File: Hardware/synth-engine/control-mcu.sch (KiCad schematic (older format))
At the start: 76 parts

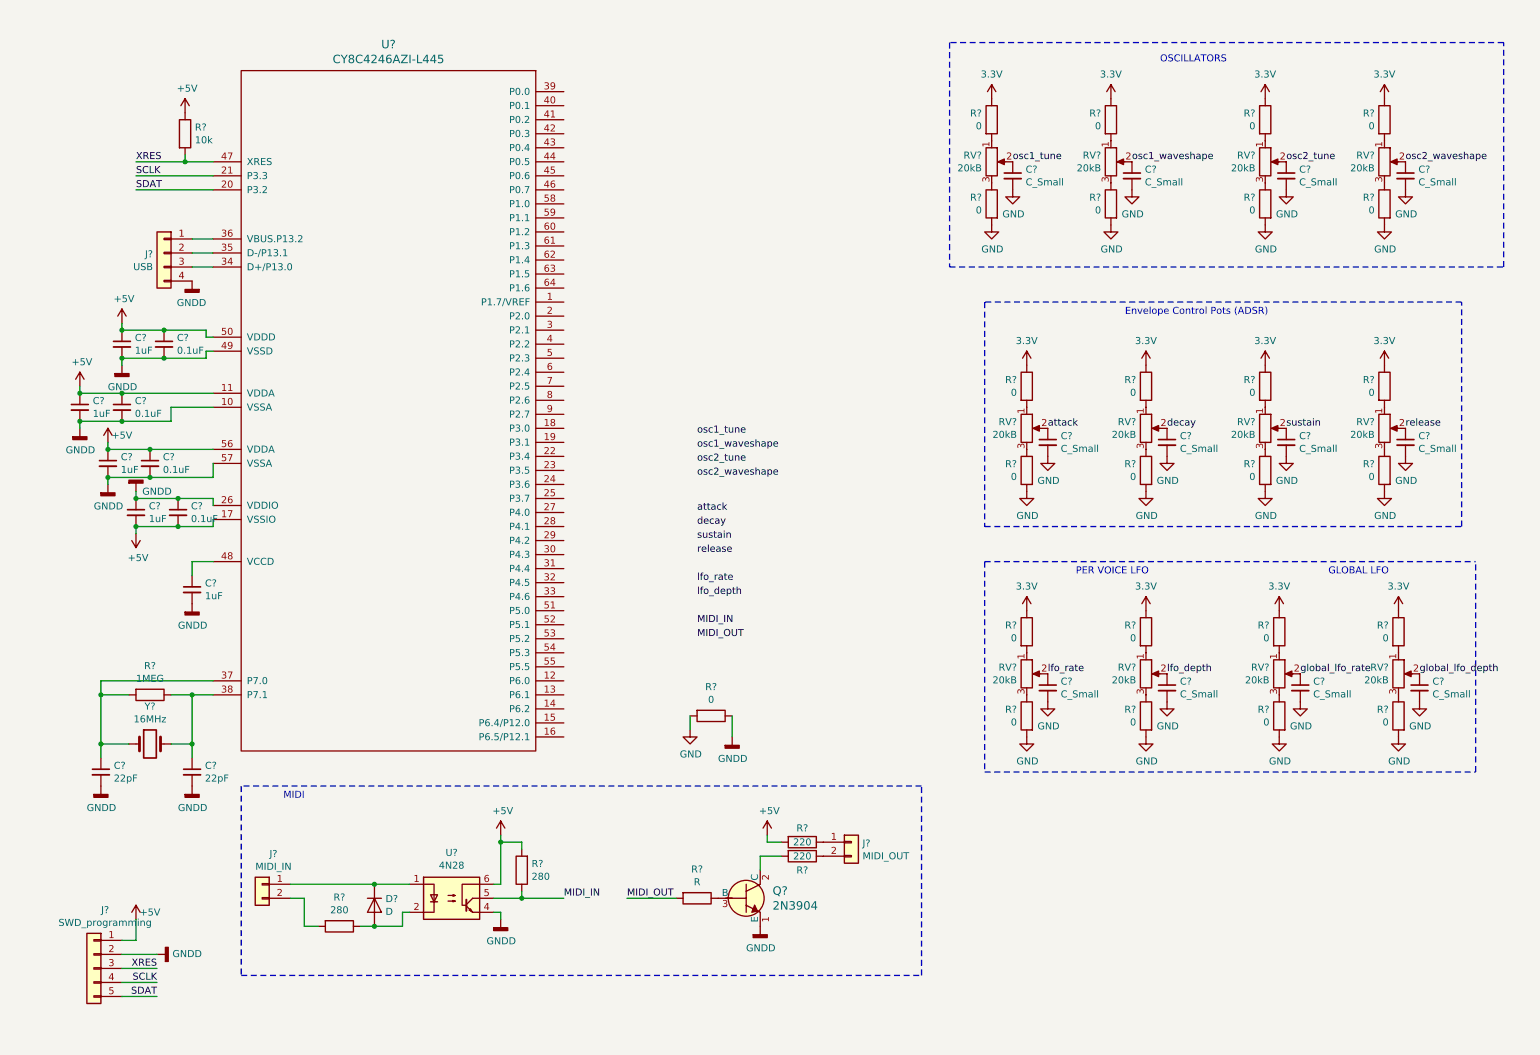
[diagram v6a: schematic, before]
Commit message: assign footprints to schematic symbols.
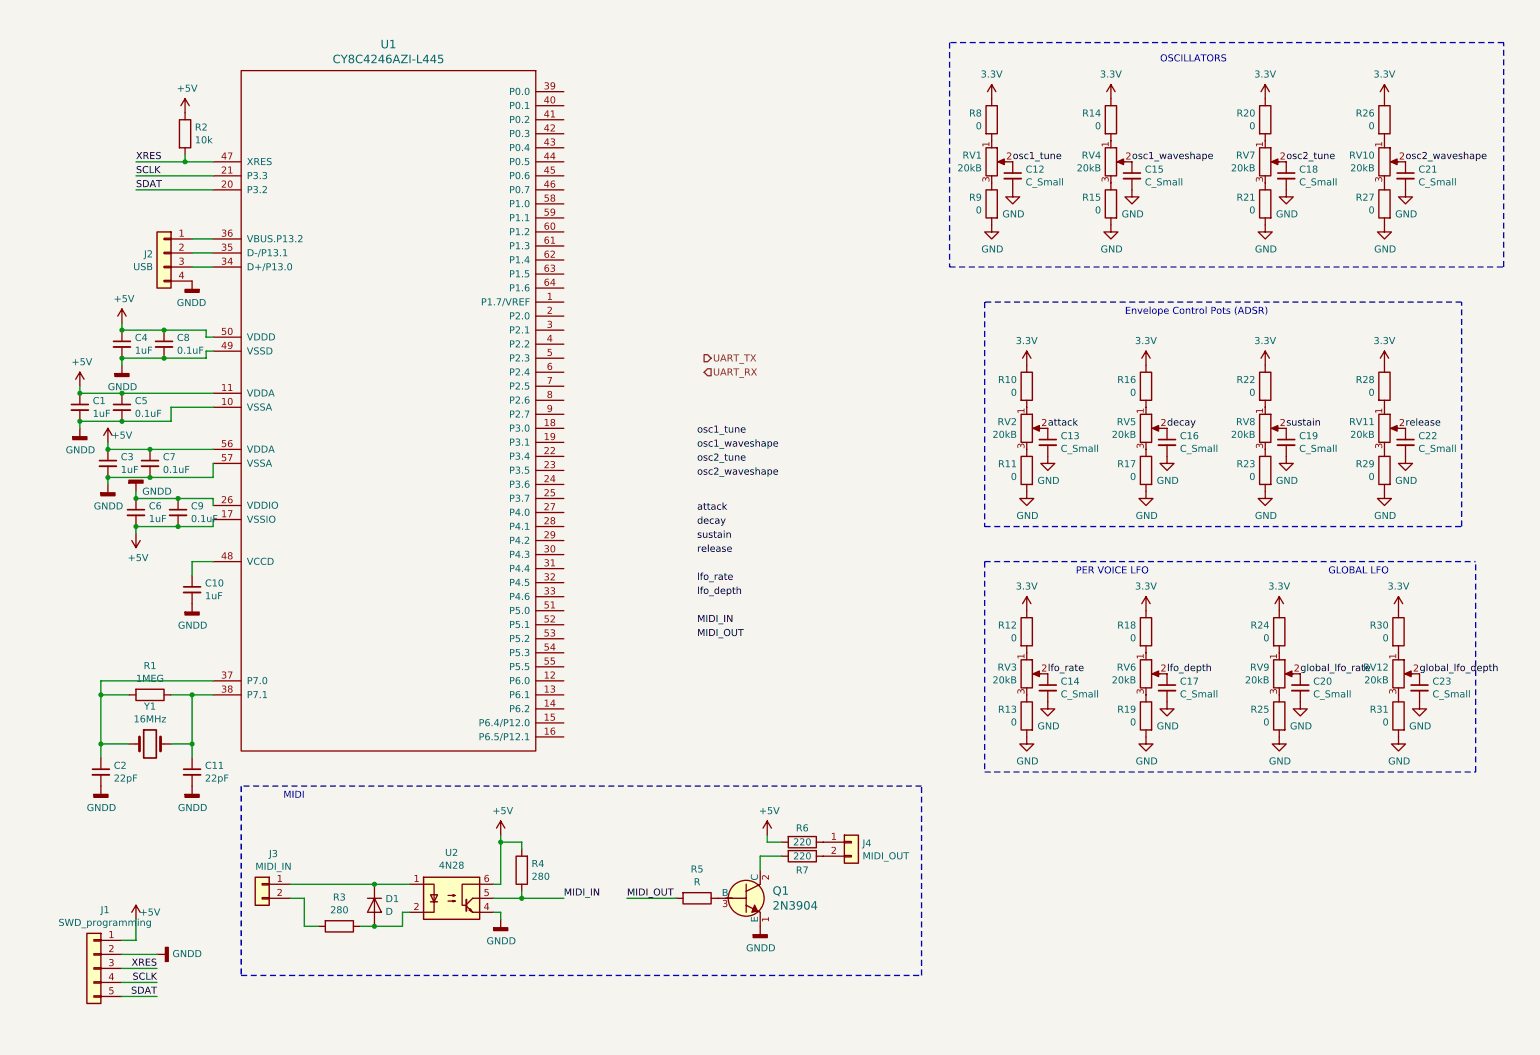
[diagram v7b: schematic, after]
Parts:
- removed R?: 0, symbol Device:R
- C1, C10, C11, C12, C13, C14, C15, C16, C17, C18, C19, C2, C20, C21, C22, C23, C3, C4, C5, C6, C7, C8, C9: renamed from C?; footprint (none) -> SparkFun-Passives:0805
- D1: renamed from D?; footprint (none) -> SparkFun-DiscreteSemi:SMA-DIODE
- J1: renamed from J?; footprint (none) -> SparkFun-Connectors:1X05
- J2: renamed from J?; footprint (none) -> SparkFun-Connectors:USB-B-PTH
- J3, J4: renamed from J?; footprint (none) -> SparkFun-Connectors:1X02
- R1, R10, R11, R12, R13, R14, R15, R16, R17, R18, R19, R2, R20, R21, R22, R23, R24, R25, R26, R27, R28, R29, R3, R30, R31, R4, R5, R6, R7, R8, R9: renamed from R?; footprint (none) -> SparkFun-Passives:0805
- RV1, RV10, RV11, RV12, RV2, RV3, RV4, RV5, RV6, RV7, RV8, RV9: renamed from RV?; footprint (none) -> Potentiometer_THT:Potentiometer_Alps_RK09K_Single_Vertical
- U1: renamed from U?; footprint (none) -> SparkFun-DigitalIC:TQFP64
- Y1: renamed from Y?; footprint (none) -> Crystal:Crystal_SMD_HC49-SD_HandSoldering
- gave numbers to parts that had none: 2

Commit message: rough placement and symbol organization. If I need to start PCB layout over from scracth, revert to this commit.
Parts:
- D1: footprint SparkFun-DiscreteSemi:SMA-DIODE -> SparkFun-DiscreteSemi:SMB-DIODE
- Q1: footprint digikey-footprints:TO-92-3 -> SparkFun-DiscreteSemi:SOT23-3
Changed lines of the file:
@@
 F 0 "D1" V 2704 6979 50  0000 L CNN
 F 1 "D" V 2795 6979 50  0000 L CNN
-F 2 "SparkFun-DiscreteSemi:SMA-DIODE" H 2750 6900 50  0001 C CNN
+F 2 "SparkFun-DiscreteSemi:SMB-DIODE" H 2750 6900 50  0001 C CNN
 F 3 "~" H 2750 6900 50  0001 C CNN
 	1    2750 6900
@@
 F 0 "Q1" H 5588 6903 60  0000 L CNN
 F 1 "2N3904" H 5588 6797 60  0000 L CNN
-F 2 "digikey-footprints:TO-92-3" H 5600 7050 60  0001 L CNN
+F 2 "SparkFun-DiscreteSemi:SOT23-3" H 5600 7050 60  0001 L CNN
 F 3 "https://my.centralsemi.com/get_document.php?cmp=1&mergetype=pd&mergepath=pd&pdf_id=LSSGP072.PDF" H 5600 7150 60  0001 L CNN
 F 4 "2N3904CS-ND" H 5600 7250 60  0001 L CNN "Digi-Key_PN"
@@
 Text Label 5050 3850 0    50   ~ 0
 osc2_waveshape
-Wire Wire Line
-	1600 2150 1450 2150
-Wire Wire Line
-	1450 2250 1600 2250
-Wire Wire Line
-	1600 2350 1450 2350
 Text HLabel 5100 3000 2    50   Output ~ 0
 UART_TX
 Text HLabel 5100 3100 2    50   Input ~ 0
 UART_RX
+Wire Wire Line
+	1450 2150 1600 2150
+Wire Wire Line
+	1450 2250 1600 2250
+Wire Wire Line
+	1450 2350 1600 2350
 $EndSCHEMATC
